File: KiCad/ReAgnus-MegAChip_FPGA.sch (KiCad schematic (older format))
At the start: 15 parts, among them J1 Conn_02x05_Odd_Even, J2 Conn_02x02_Odd_Even, U10 AS4C4M16SA, U11 74LVC245A, U12 74LVC1GX04, U7 GW1N-UV9LQ144, X1 SG-8002CA, Y1 CL=16pF

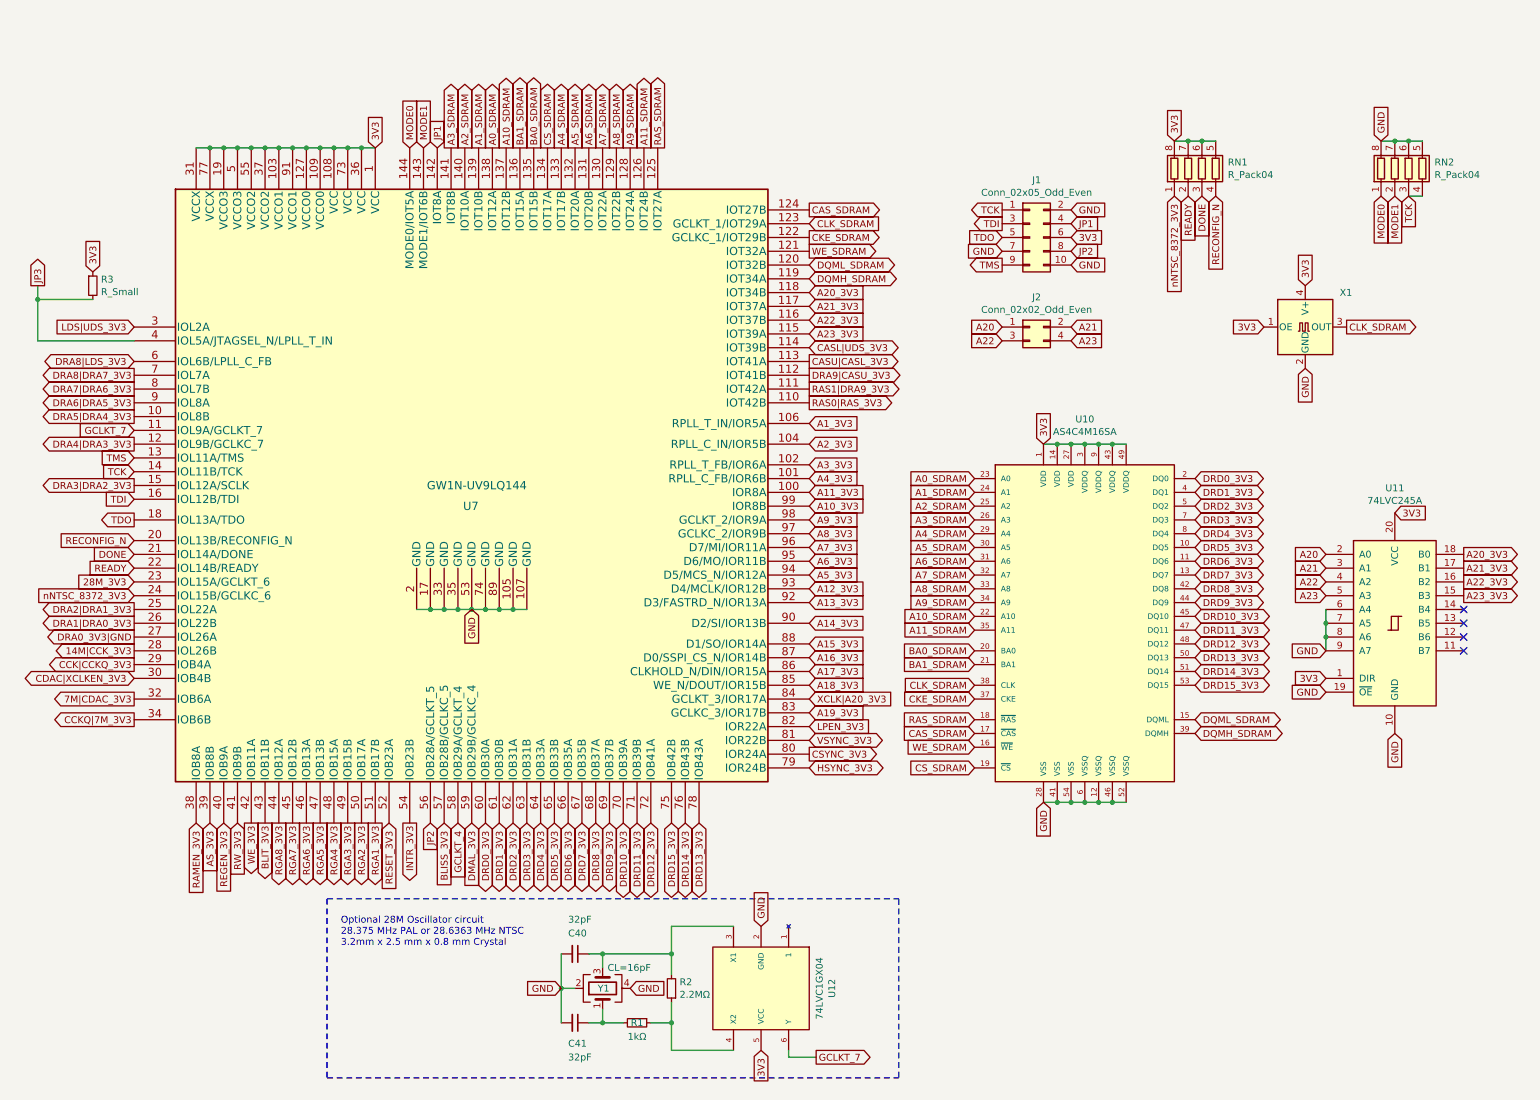
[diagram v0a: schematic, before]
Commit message: Removed the SDRAM chip and the crystal oscillator
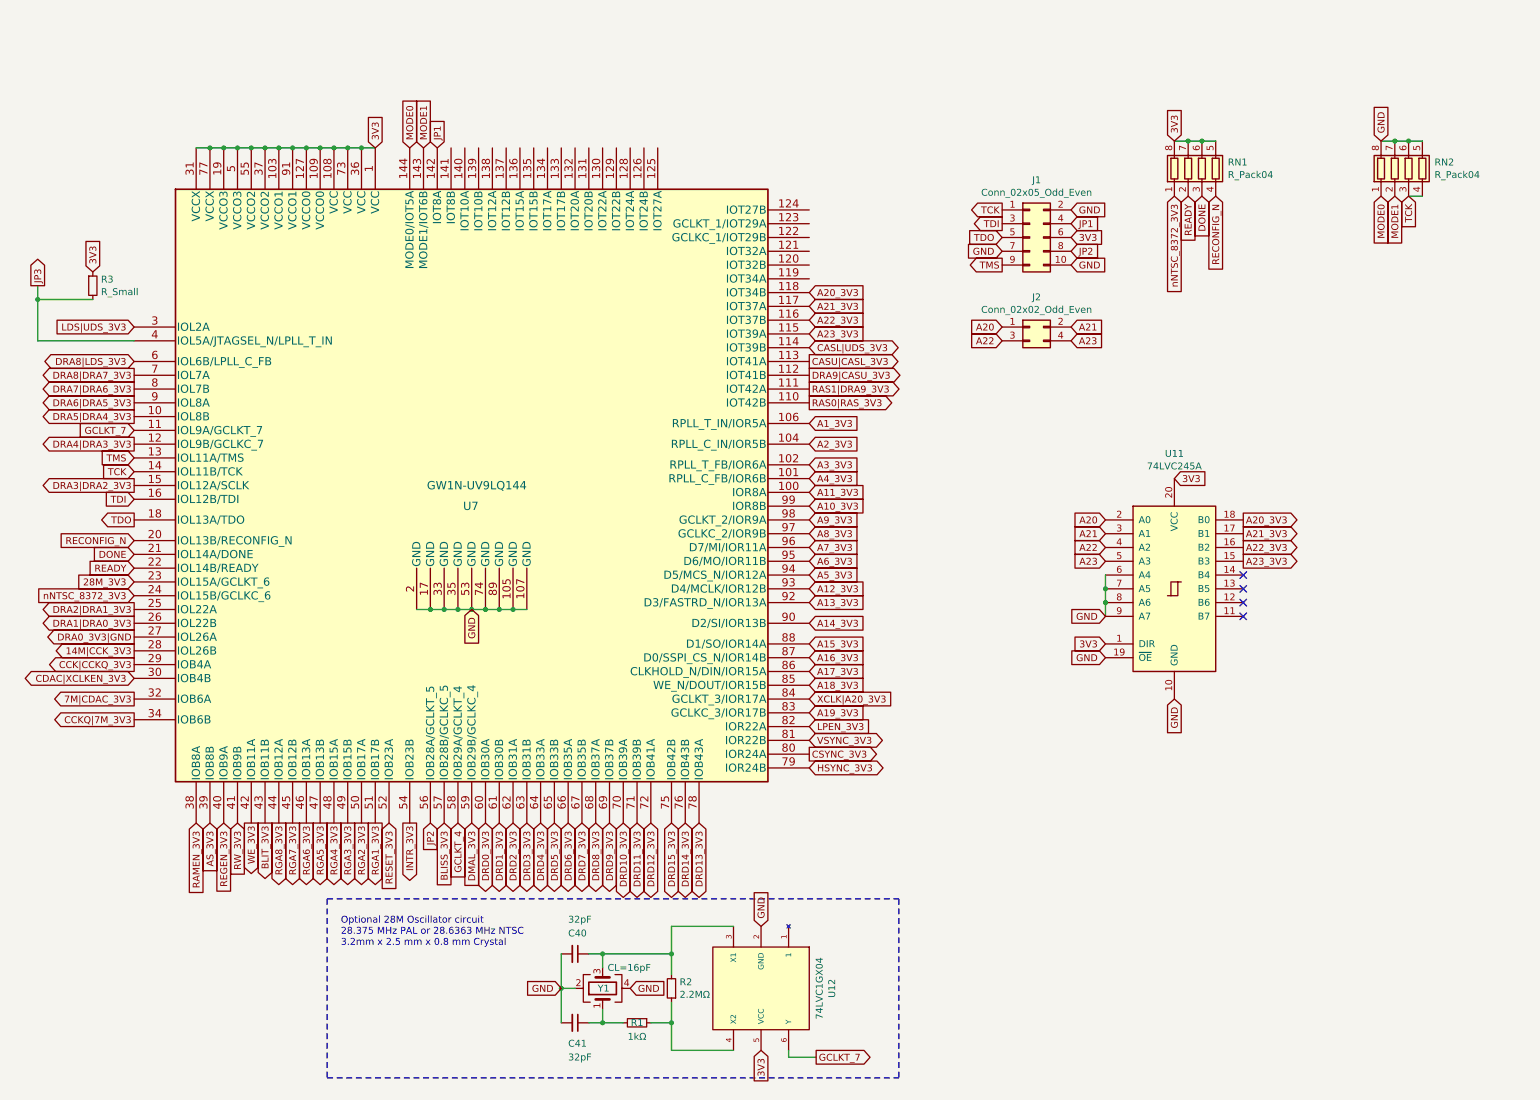
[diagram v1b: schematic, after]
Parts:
- removed U10: AS4C4M16SA, Package_SO:TSOP-II-54_22.2x10.16mm_P0.8mm, symbol Memory_RAM:AS4C4M16SA
- removed X1: SG-8002CA, Oscillator:Oscillator_SMD_SeikoEpson_SG8002CA-4Pin_7.0x5.0mm, symbol ReAgnus-MegAChip:SG-8002CA-Oscillator
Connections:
- net A0_SDRAM: no longer names the net of U7.138 (IOT12A)
- net A10_SDRAM: no longer names the net of U7.137 (IOT12B)
- net A11_SDRAM: no longer names the net of U7.126 (IOT24B)
- net A1_SDRAM: no longer names the net of U7.139 (IOT10B)
- net A2_SDRAM: no longer names the net of U7.140 (IOT10A)
- net A3_SDRAM: no longer names the net of U7.141 (IOT8B)
- net A4_SDRAM: no longer names the net of U7.133 (IOT17B)
- net A5_SDRAM: no longer names the net of U7.132 (IOT20A)
- net A6_SDRAM: no longer names the net of U7.131 (IOT20B)
- net A7_SDRAM: no longer names the net of U7.130 (IOT22A)
- net A8_SDRAM: no longer names the net of U7.129 (IOT22B)
- net A9_SDRAM: no longer names the net of U7.128 (IOT24A)
- net BA0_SDRAM: no longer names the net of U7.135 (IOT15B)
- net BA1_SDRAM: no longer names the net of U7.136 (IOT15A)
- net CAS_SDRAM: no longer names the net of U7.124 (IOT27B)
- net CKE_SDRAM: no longer names the net of U7.122 (GCLKC_1/IOT29B)
- net CLK_SDRAM: no longer names the net of U7.123 (GCLKT_1/IOT29A)
- net CS_SDRAM: no longer names the net of U7.134 (IOT17A)
- net DQMH_SDRAM: no longer names the net of U7.119 (IOT34A)
- net DQML_SDRAM: no longer names the net of U7.120 (IOT32B)
- net RAS_SDRAM: no longer names the net of U7.125 (IOT27A)
- net WE_SDRAM: no longer names the net of U7.121 (IOT32A)
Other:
- moved on the sheet: U11

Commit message: Went to a 4-layer PCB and changed FPGA to GW1NR-UV9LQ144P with embedded PSRAM, changed FET-bus-switches to SN74CBT16210CDGVR (TVSOP-48) and added 4.3V LDO regulator TPS73643DBV and re-routed.
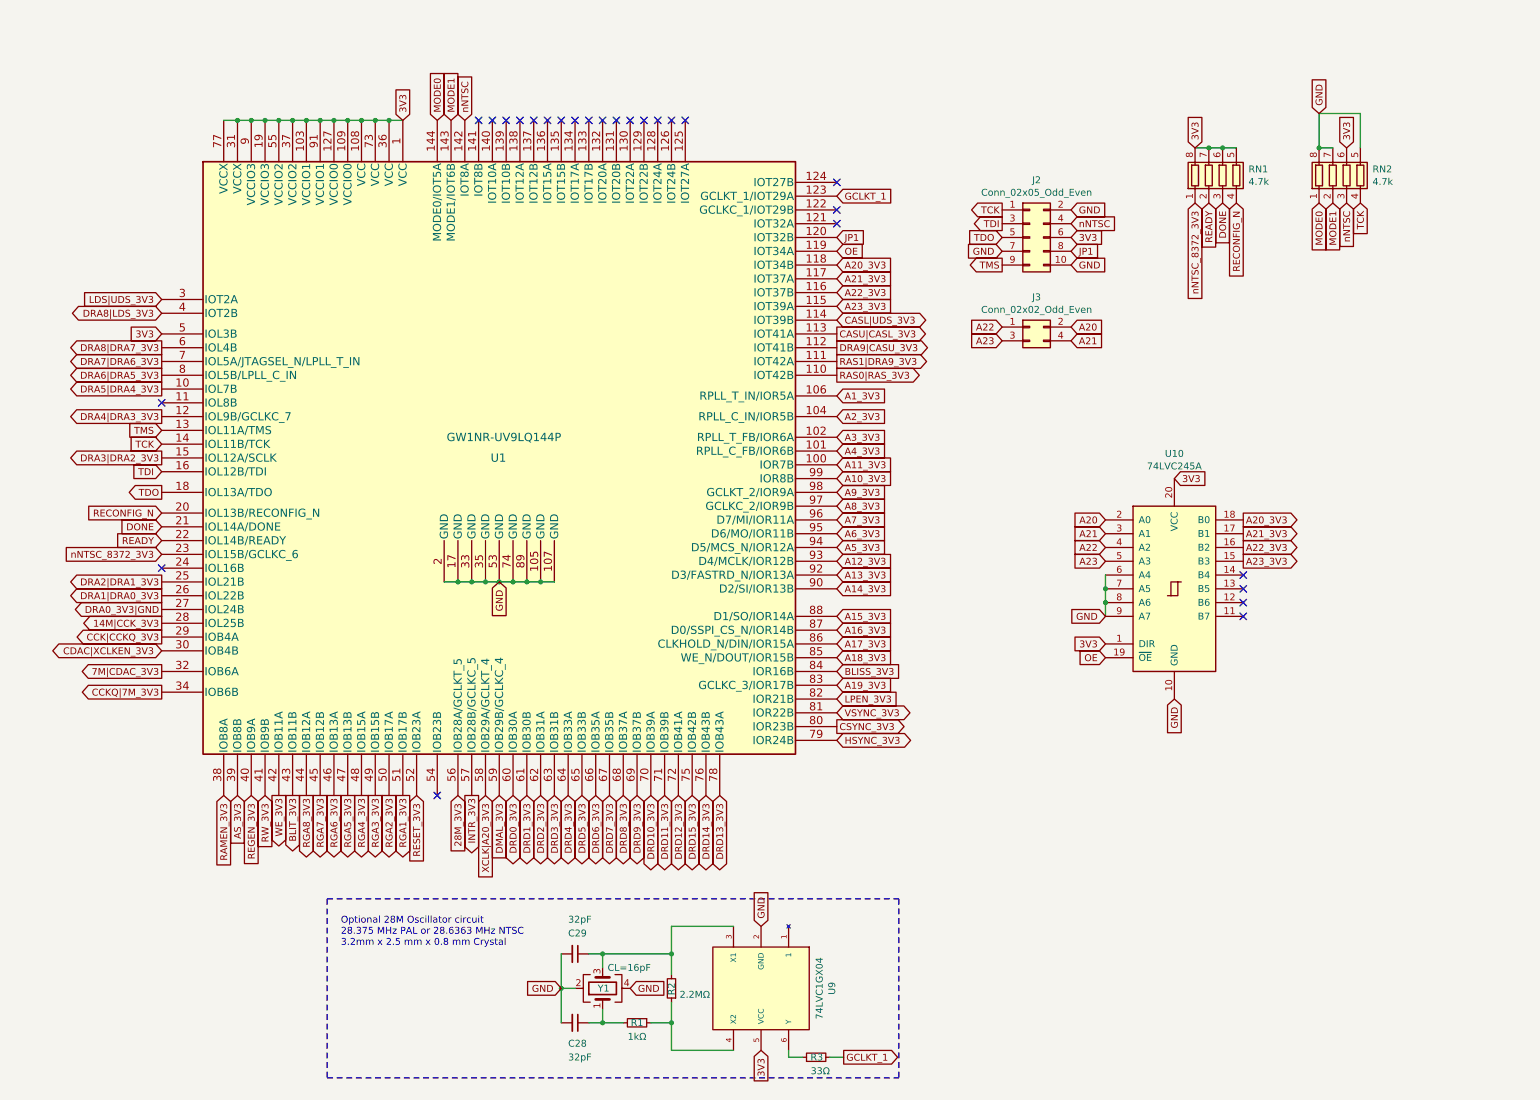
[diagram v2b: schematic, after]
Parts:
- removed U7: GW1N-UV9LQ144, Package_QFP:LQFP-144_20x20mm_P0.5mm, symbol ReAgnus-MegAChip:GW1N-UV9LQ144
- added U1: GW1NR-UV9LQ144P, Package_QFP:LQFP-144_20x20mm_P0.5mm, symbol ReAgnus-MegAChip:GW1NR-UV9LQ144P
- R3: value R_Small -> 33Ω; footprint Resistor_SMD:R_0805_2012Metric_Pad1.15x1.40mm_HandSolder -> Resistor_SMD:R_0603_1608Metric_Pad0.98x0.95mm_HandSolder
- RN1, RN2: value R_Pack04 -> 4.7k
- renumbered C41 to C28, C40 to C29, J1 to J2, J2 to J3, U11 to U10, U12 to U9
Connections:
- net JP2 is gone; now on net JP1: J2.8 (Pin_8)
- net 14M|CCK_3V3: now also U1.28 (IOL25B)
- net 28M_3V3: now also U1.56 (IOB28A/GCLKT_5)
- net 3V3: now also RN2.6 (R3.2), U1.1 (VCC), U1.103 (VCCIO1), U1.108 (VCC), U1.109 (VCCIO0), U1.127 (VCCIO0), U1.19 (VCCIO3), U1.31 (VCCX), U1.36 (VCC), U1.37 (VCCIO2), U1.5 (IOL3B), U1.55 (VCCIO2), U1.73 (VCC), U1.77 (VCCX), U1.9 (VCCIO3), U1.91 (VCCIO1); no longer R3.1
- net 7M|CDAC_3V3: now also U1.32 (IOB6A)
- net A10_3V3: now also U1.99 (IOR8B)
- net A11_3V3: now also U1.100 (IOR7B)
- net A12_3V3: now also U1.93 (D4/MCLK/IOR12B)
- net A13_3V3: now also U1.92 (D3/FASTRD_N/IOR13A)
- net A14_3V3: now also U1.90 (D2/SI/IOR13B)
- net A15_3V3: now also U1.88 (D1/SO/IOR14A)
- net A16_3V3: now also U1.87 (D0/SSPI_CS_N/IOR14B)
- net A17_3V3: now also U1.86 (CLKHOLD_N/DIN/IOR15A)
- net A18_3V3: now also U1.85 (WE_N/DOUT/IOR15B)
- net A19_3V3: now also U1.83 (GCLKC_3/IOR17B)
- net A1_3V3: now also U1.106 (RPLL_T_IN/IOR5A)
- net A20: now also J3.2 (Pin_2); no longer J3.1 (Pin_1)
- net A20_3V3: now also U1.118 (IOT34B)
- net A21: now also J3.4 (Pin_4); no longer J3.2 (Pin_2)
- net A21_3V3: now also U1.117 (IOT37A)
- net A22: now also J3.1 (Pin_1); no longer J3.3 (Pin_3)
- net A22_3V3: now also U1.116 (IOT37B)
- net A23: now also J3.3 (Pin_3); no longer J3.4 (Pin_4)
- net A23_3V3: now also U1.115 (IOT39A)
- net A2_3V3: now also U1.104 (RPLL_C_IN/IOR5B)
- net A3_3V3: now also U1.102 (RPLL_T_FB/IOR6A)
- net A4_3V3: now also U1.101 (RPLL_C_FB/IOR6B)
- net A5_3V3: now also U1.94 (D5/MCS_N/IOR12A)
- net A6_3V3: now also U1.95 (D6/MO/IOR11B)
- net A7_3V3: now also U1.96 (D7/MI/IOR11A)
- net A8_3V3: now also U1.97 (GCLKC_2/IOR9B)
- net A9_3V3: now also U1.98 (GCLKT_2/IOR9A)
- net AS_3V3: now also U1.39 (IOB8B)
- net BLISS_3V3: now also U1.84 (IOR16B)
- net BLIT_3V3: now also U1.43 (IOB11B)
- net CASL|UDS_3V3: now also U1.114 (IOT39B)
- net CASU|CASL_3V3: now also U1.113 (IOT41A)
- net CCKQ|7M_3V3: now also U1.34 (IOB6B)
- net CCK|CCKQ_3V3: now also U1.29 (IOB4A)
- net CDAC|XCLKEN_3V3: now also U1.30 (IOB4B)
- net CSYNC_3V3: now also U1.80 (IOR23B)
- net DMAL_3V3: now also U1.59 (IOB29B/GCLKC_4)
- net DONE: now also U1.21 (IOL14A/DONE)
- net DRA0_3V3|GND: now also U1.27 (IOL24B)
- net DRA1|DRA0_3V3: now also U1.26 (IOL22B)
- net DRA2|DRA1_3V3: now also U1.25 (IOL21B)
- net DRA3|DRA2_3V3: now also U1.15 (IOL12A/SCLK)
- net DRA4|DRA3_3V3: now also U1.12 (IOL9B/GCLKC_7)
- net DRA5|DRA4_3V3: now also U1.10 (IOL7B)
- net DRA6|DRA5_3V3: now also U1.8 (IOL5B/LPLL_C_IN)
- net DRA7|DRA6_3V3: now also U1.7 (IOL5A/JTAGSEL_N/LPLL_T_IN)
- net DRA8|DRA7_3V3: now also U1.6 (IOL4B)
- net DRA8|LDS_3V3: now also U1.4 (IOT2B)
- net DRA9|CASU_3V3: now also U1.112 (IOT41B)
- net DRD0_3V3: now also U1.60 (IOB30A)
- net DRD10_3V3: now also U1.70 (IOB39A)
- net DRD11_3V3: now also U1.71 (IOB39B)
- net DRD12_3V3: now also U1.72 (IOB41A)
- net DRD13_3V3: now also U1.78 (IOB43A)
- net DRD14_3V3: now also U1.76 (IOB43B)
- net DRD15_3V3: now also U1.75 (IOB42B)
- net DRD1_3V3: now also U1.61 (IOB30B)
- net DRD2_3V3: now also U1.62 (IOB31A)
- net DRD3_3V3: now also U1.63 (IOB31B)
- net DRD4_3V3: now also U1.64 (IOB33A)
- net DRD5_3V3: now also U1.65 (IOB33B)
- net DRD6_3V3: now also U1.66 (IOB35A)
- net DRD7_3V3: now also U1.67 (IOB35B)
- net DRD8_3V3: now also U1.68 (IOB37A)
- net DRD9_3V3: now also U1.69 (IOB37B)
- net GND: now also U1.105 (GND), U1.107 (GND), U1.17 (GND), U1.2 (GND), U1.33 (GND), U1.35 (GND), U1.53 (GND), U1.74 (GND), U1.89 (GND); no longer RN2.6 (R3.2), U10.19 (~OE)
- net HSYNC_3V3: now also U1.79 (IOR24B)
- net INTR_3V3: now also U1.57 (IOB28B/GCLKC_5)
- net JP1: now also U1.120 (IOT32B); no longer J2.4 (Pin_4)
- net LDS|UDS_3V3: now also U1.3 (IOT2A)
- net LPEN_3V3: now also U1.82 (IOR21B)
- net MODE0: now also U1.144 (MODE0/IOT5A)
- net MODE1: now also U1.143 (MODE1/IOT6B)
- net RAMEN_3V3: now also U1.38 (IOB8A)
- net RAS0|RAS_3V3: now also U1.110 (IOT42B)
- net RAS1|DRA9_3V3: now also U1.111 (IOT42A)
- net READY: now also U1.22 (IOL14B/READY)
- net RECONFIG_N: now also U1.20 (IOL13B/RECONFIG_N)
- net REGEN_3V3: now also U1.40 (IOB9A)
- net RESET_3V3: now also U1.52 (IOB23A)
- net RGA1_3V3: now also U1.51 (IOB17B)
- net RGA2_3V3: now also U1.50 (IOB17A)
- net RGA3_3V3: now also U1.49 (IOB15B)
- net RGA4_3V3: now also U1.48 (IOB15A)
- net RGA5_3V3: now also U1.47 (IOB13B)
- net RGA6_3V3: now also U1.46 (IOB13A)
- net RGA7_3V3: now also U1.45 (IOB12B)
- net RGA8_3V3: now also U1.44 (IOB12A)
- net RW_3V3: now also U1.41 (IOB9B)
- net TCK: now also U1.14 (IOL11B/TCK); no longer RN2.3 (R3.1)
- net TDI: now also U1.16 (IOL12B/TDI)
- net TDO: now also U1.18 (IOL13A/TDO)
- net TMS: now also U1.13 (IOL11A/TMS)
- net VSYNC_3V3: now also U1.81 (IOR22B)
- net WE_3V3: now also U1.42 (IOB11A)
- net XCLK|A20_3V3: now also U1.58 (IOB29A/GCLKT_4)
- net nNTSC_8372_3V3: now also U1.23 (IOL15B/GCLKC_6)
- net GCLKT_7: no longer names the net of U9.6 (Y)
- net GCLKT_7: now also R3.1
- net JP3 renamed GCLKT_1
- net GCLKT_1: now also U1.123 (GCLKT_1/IOT29A)
- new net OE: U1.119 (IOT34A), U10.19 (~OE)
- new net nNTSC: J2.4 (Pin_4), RN2.3 (R3.1), U1.142 (IOT8A)
- no-connect marks 4 -> 26
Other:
- moved on the sheet: R3, RN1

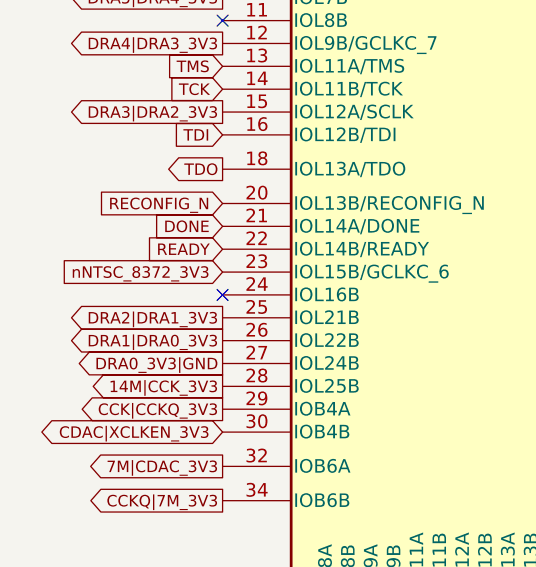
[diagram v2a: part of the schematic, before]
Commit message: Moved signal nNTSC_8372_3V3 to pin FPGA pin 24
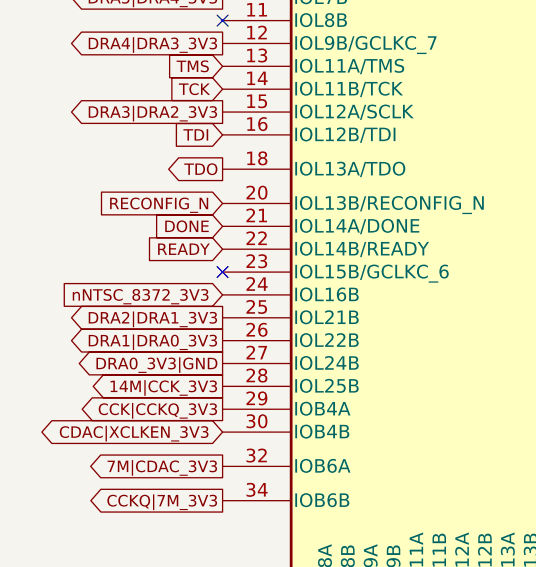
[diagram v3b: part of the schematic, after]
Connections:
- net nNTSC_8372_3V3: now also U1.24 (IOL16B); no longer U1.23 (IOL15B/GCLKC_6)
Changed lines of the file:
@@
 Text GLabel 3500 850  1    50   Input ~ 0
 MODE0
-Text GLabel 1500 4000 0    50   Input ~ 0
+Text GLabel 1500 4100 0    50   Input ~ 0
 nNTSC_8372_3V3
 Text GLabel 3700 850  1    50   Input ~ 0
@@
 Text GLabel 10100 1450 3    50   Input ~ 0
 nNTSC
-NoConn ~ 1500 4100
+NoConn ~ 1500 4000
 NoConn ~ 1500 2900
 $EndSCHEMATC
